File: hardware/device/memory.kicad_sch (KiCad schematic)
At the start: 2 parts, among them IC2 IS42S16160J-7BLI, J3 Micro_SD_Card_Det_Hirose_DM3AT

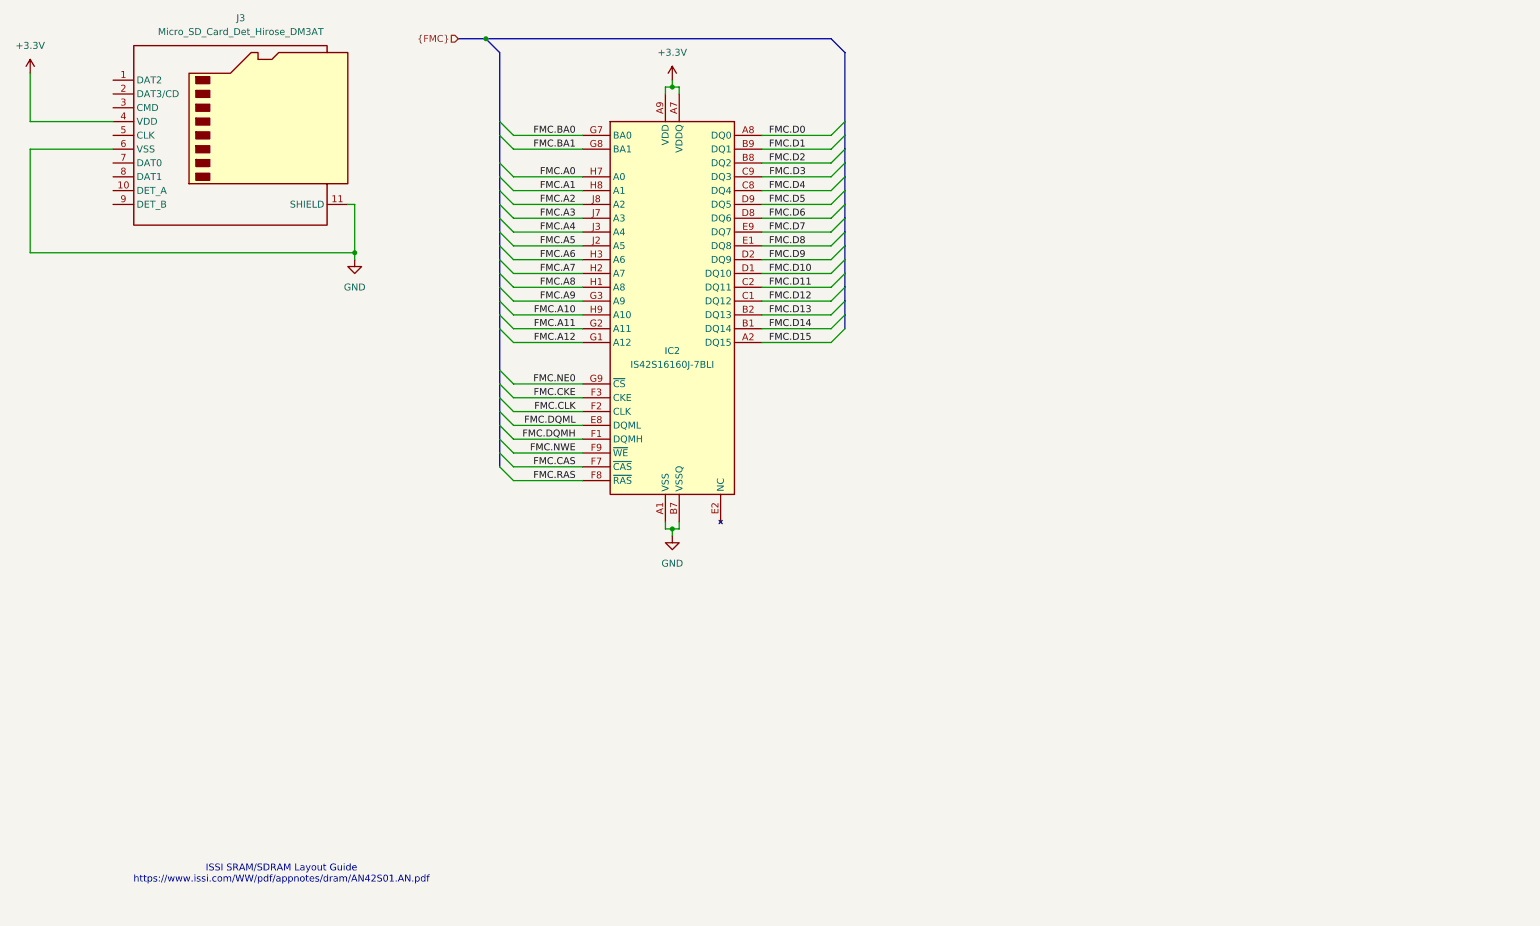
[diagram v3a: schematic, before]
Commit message: feat: BGA routing for SDRAM
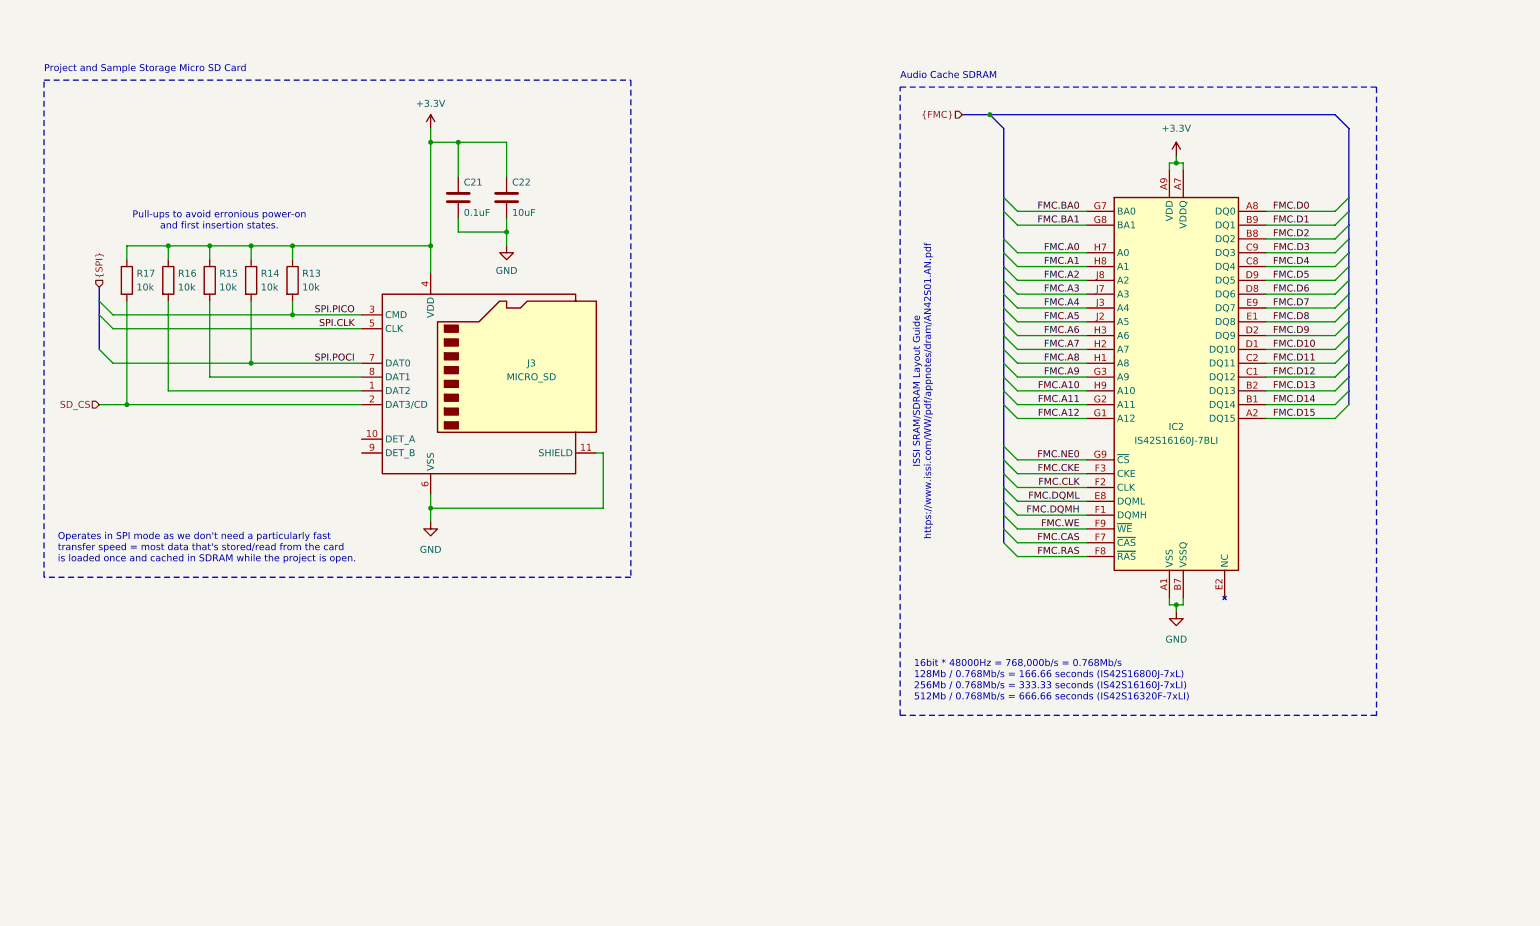
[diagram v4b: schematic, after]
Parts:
- added C21: 0.1uF, Capacitor_SMD:C_0603_1608Metric_Pad1.08x0.95mm_HandSolder, symbol Device:C
- added C22: 10uF, Capacitor_SMD:C_0603_1608Metric_Pad1.08x0.95mm_HandSolder, symbol Device:C
- added R13, R14, R15, R16, R17: 10k, symbol Device:R
- J3: value Micro_SD_Card_Det_Hirose_DM3AT -> MICRO_SD
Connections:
- net +3.3V: now also C21.1, C22.1, R13.1, R14.1, R15.1, R16.1, R17.1
- net GND: now also C21.2, C22.2
- net at J3.1 (DAT2): now also R16.2
- net SD_CS: now reaches J3.2 (DAT3/CD)
- net SD_CS: now also R17.2
- net SPI.PICO: now reaches J3.3 (CMD)
- net SPI.PICO: now also R13.2
- net SPI.CLK: now reaches J3.5 (CLK)
- net SPI.POCI: now reaches J3.7 (DAT0)
- net SPI.POCI: now also R14.2
- net at J3.8 (DAT1): now also R15.2
- net FMC.NWE renamed FMC.WE
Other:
- note added: "16bit * 48000Hz = 768,000b/s = 0.768Mb/s 128Mb / 0.768Mb/s = 166.66 seconds (IS42S16800J-7xL) 256Mb / 0.768Mb/s = 333.33 seconds (IS42S16160J-7xLI) 512Mb / 0.768Mb/s = 666.66 seconds (IS42S16320F-7xLI)"
- note added: "Audio Cache SDRAM"
- note added: "Operates in SPI mode as we don't need a particularly fast transfer speed = most data that's stored/read from the card is loaded once and cached in SDRAM while the project is open."
- note added: "Project and Sample Storage Micro SD Card"
- note added: "Pull-ups to avoid erronious power-on and first insertion states."
- moved on the sheet: IC2, J3

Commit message: feat: various audio and power schematic layout
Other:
- moved on the sheet: C21, C22, IC2, J3, R13, R14, R15, R16, R17

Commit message: feat: fit SD card and SPI bus to layout
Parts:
- J3: footprint Connector_Card:microSD_HC_Hirose_DM3BT-DSF-PEJS -> Connector_Card:microSD_HC_Hirose_DM3AT-SF-PEJM5
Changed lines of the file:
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@@
 			)
 		)
-		(property "Footprint" "Connector_Card:microSD_HC_Hirose_DM3BT-DSF-PEJS"
+		(property "Footprint" "Connector_Card:microSD_HC_Hirose_DM3AT-SF-PEJM5"
 			(at 158.75 63.5 0)
 			(effects

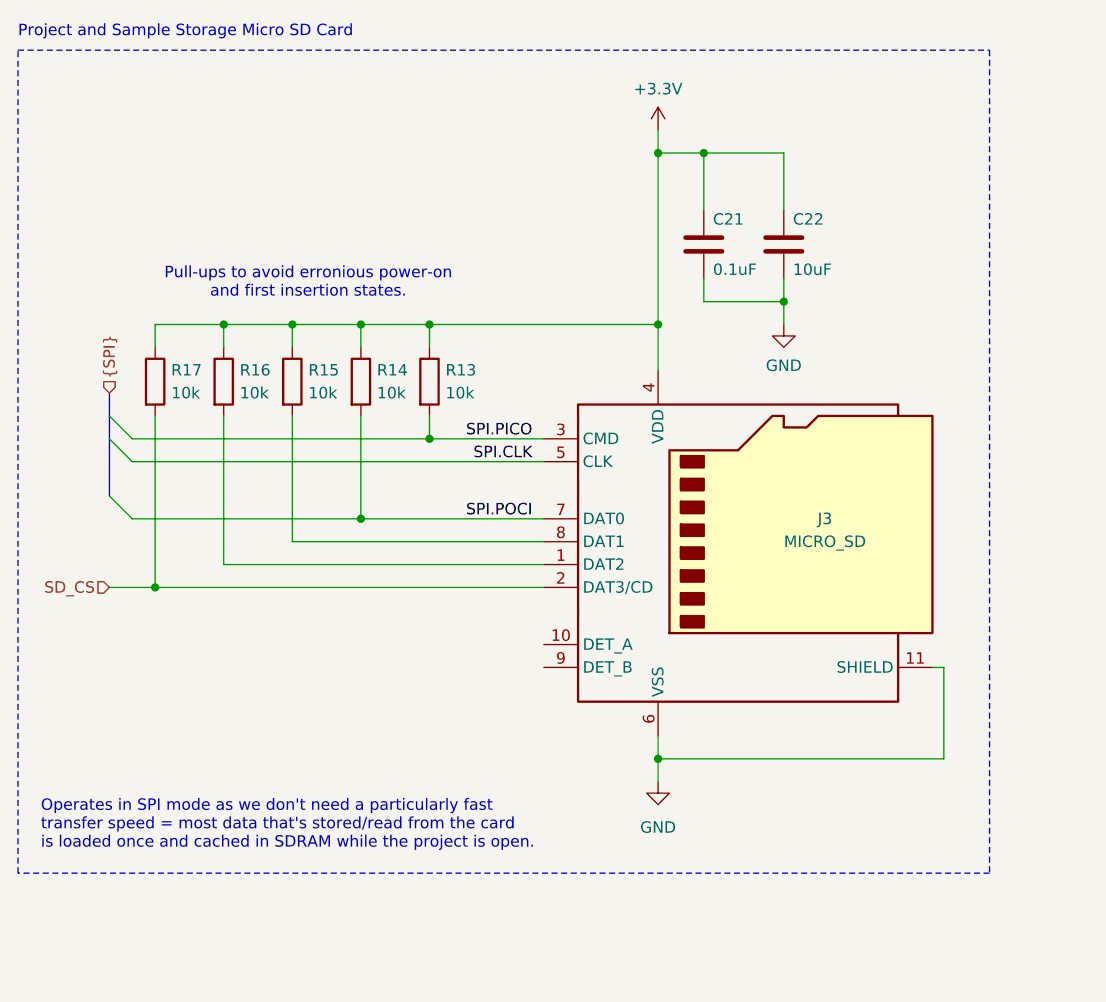
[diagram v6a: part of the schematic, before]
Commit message: feat: various layout, start adding capacitive pads
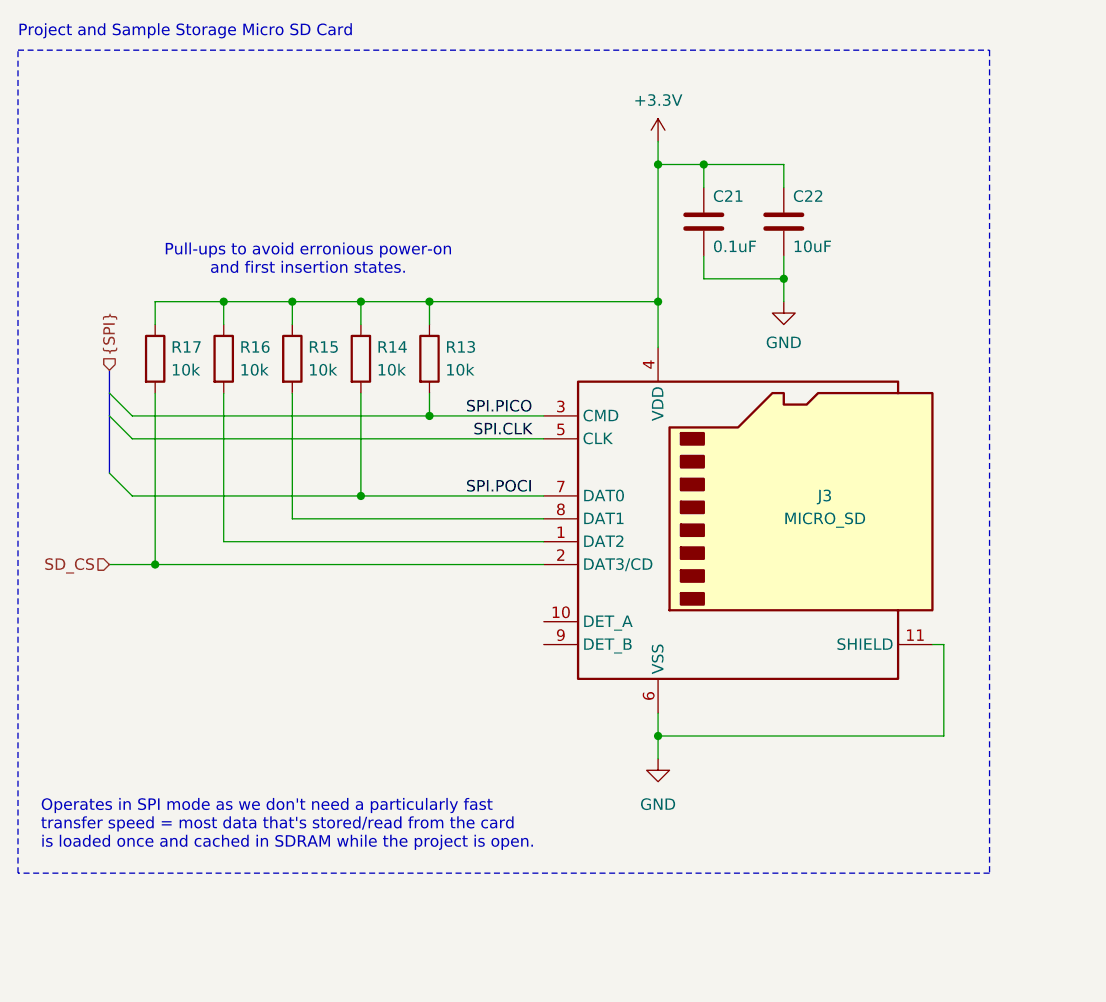
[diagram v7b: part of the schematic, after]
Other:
- moved on the sheet: C21, C22, J3, R13, R14, R15, R16, R17

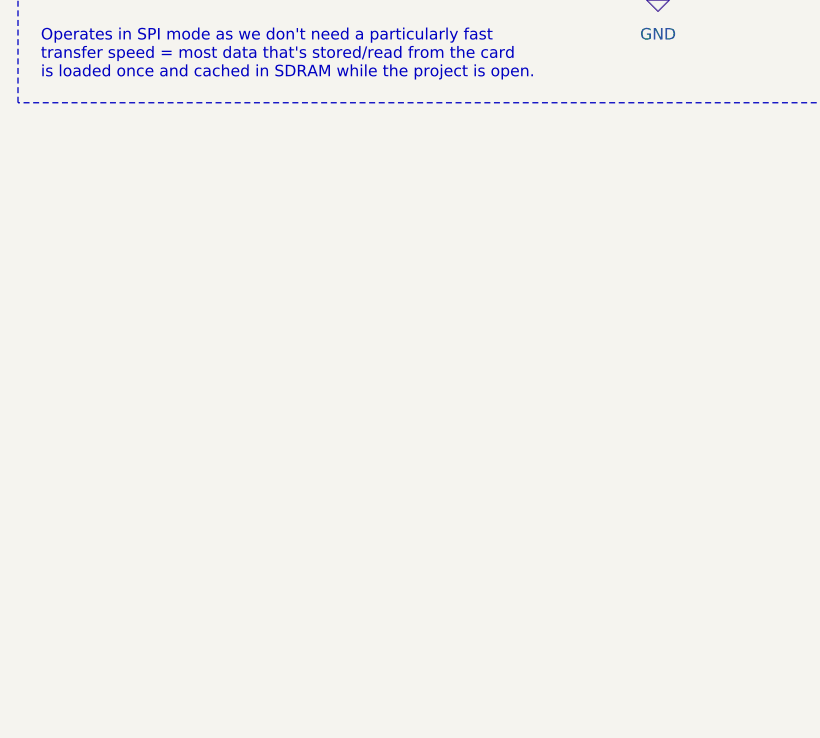
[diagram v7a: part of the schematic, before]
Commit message: feat: add integrated flash memory
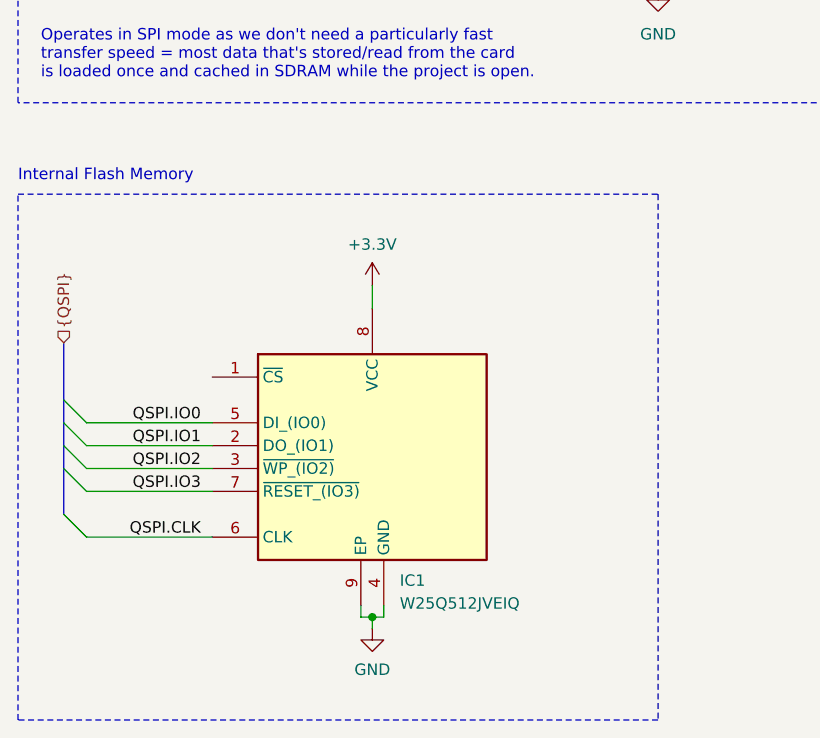
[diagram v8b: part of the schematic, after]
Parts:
- added IC1: W25Q512JVEIQ, pocket_synth:W25Q512JVEIQ, symbol pocket_synth:W25Q512JVEIQ
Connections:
- net +3.3V: now also IC1.8 (VCC)
- net GND: now also IC1.4 (GND), IC1.9 (EP)
- new net QSPI.CLK: IC1.6 (CLK)
- new net QSPI.IO0: IC1.5 (DI_(IO0))
- new net QSPI.IO1: IC1.2 (DO_(IO1))
- new net QSPI.IO2: IC1.3 (~{WP_(IO2)})
- new net QSPI.IO3: IC1.7 (~{RESET_(IO3)})
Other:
- note added: "Internal Flash Memory"
